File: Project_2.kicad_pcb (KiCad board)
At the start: 4 copper layers, 82 x 58.4 mm, 154 parts, among them CON3 BARREL_JACK, J1 USB, P1 CONN_01X10, P2 CONN_01X02, Q1 RTQ020N03, Q2 RTQ020N03, Q3 RTQ020N03, Q4 RTQ020N03, Q5 RTQ020N03, U1 LM2675_Adj, U2 LM2675_5V, U3 SM72442, U4 SM72295, U5 TLV2371_DBV

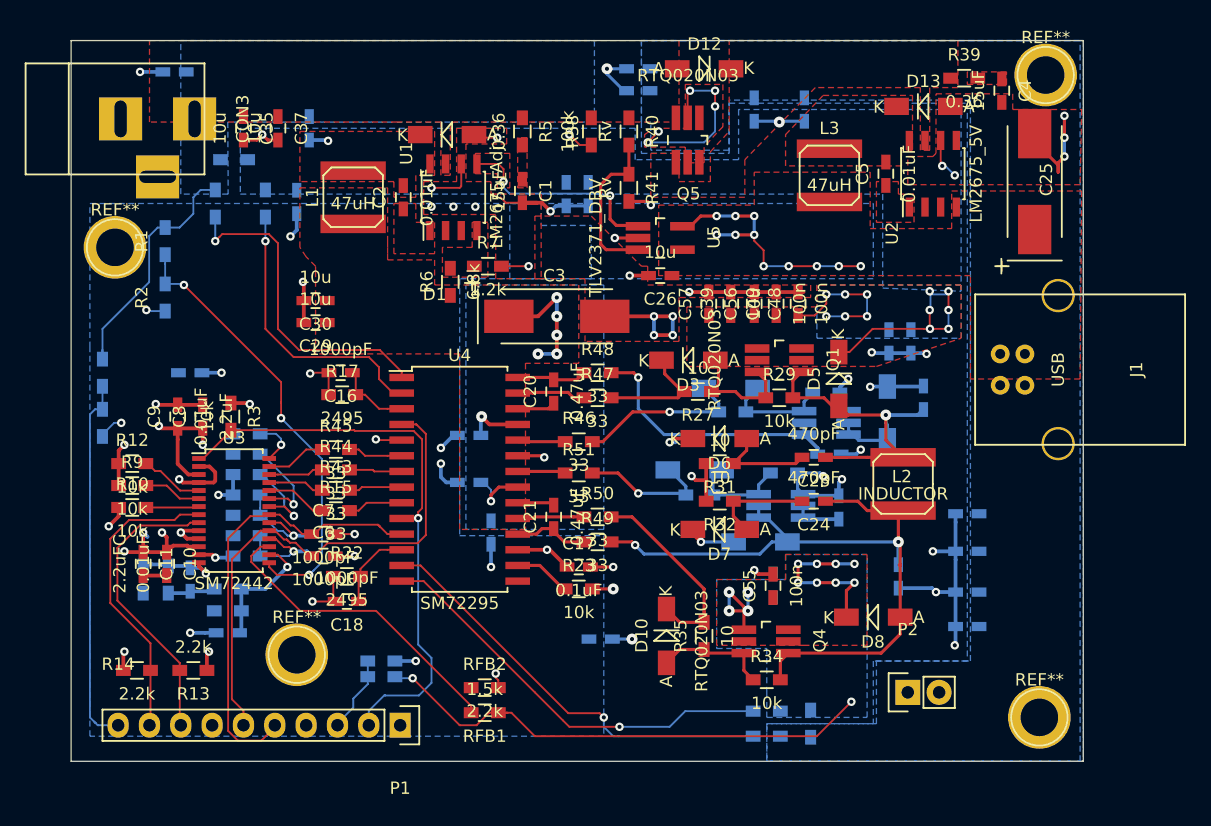
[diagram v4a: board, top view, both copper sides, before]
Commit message: Cleared all DRC errors.
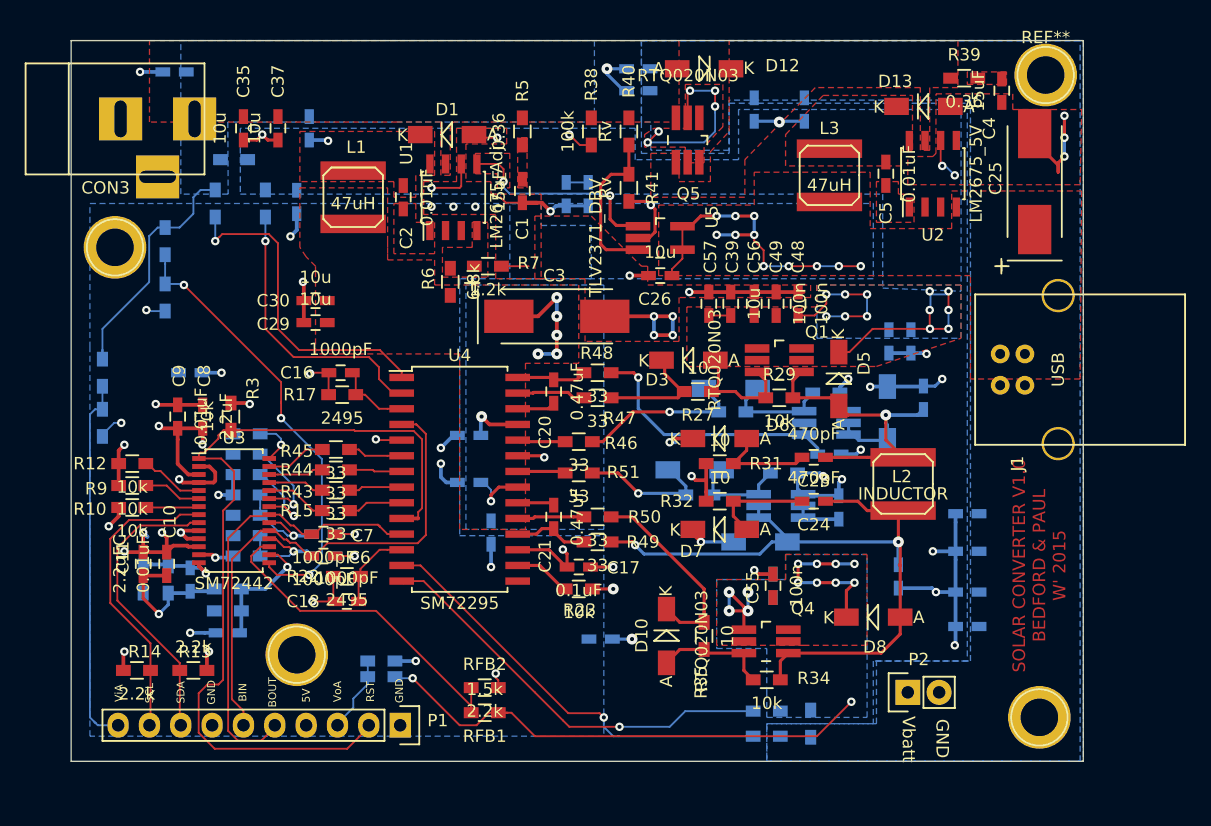
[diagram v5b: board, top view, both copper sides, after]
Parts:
- renumbered REF** to ?
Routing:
- net /Connectors/RST: track 48.4 -> 69.4 mm, vias 1 -> 0
- net GNDD: track 193.8 -> 201.8 mm, vias 63 -> 62
- net 5VDC: track 54.7 -> 60.3 mm
- net Vin: track 28.6 -> 32.2 mm
- net Net-(RFB1-Pad2): track 25.4 -> 27.4 mm
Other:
- board text added: "5V"
- board text added: "BIN"
- board text added: "BOUT"
- board text added: "GND"
- board text added: "RST"
- board text added: "SCL"
- board text added: "SDA"
- board text added: "SOLAR CONVERTER V1.0 BEDFORD & PAUL W' 2015"
- board text added: "Vbatt"
- board text added: "ViA"
- board text added: "VoA"

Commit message: updated via placement for better ground plane continuity
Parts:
- moved ? 1.09 mm to (135.4, 137.8)
- moved REF** 0.77 mm to (135.6, 85.5)
- moved C25 0.40 mm to (133.9, 94.4)
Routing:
- net 8VDC: track 20.5 -> 30.2 mm, vias 7 -> 8
- net GNDD: track 201.8 -> 206.9 mm
- net /HBridge/HSA: track 52.5 -> 56.1 mm
- net /HBridge/HSB: track 63.5 -> 67.1 mm
- net 5VDC: track 60.3 -> 57.5 mm, vias 21 -> 18
- net Vin: track 32.2 -> 29.4 mm, vias 12 -> 10
- net Vout: track 63.0 -> 65.2 mm
- net (no net): track 0.72 -> 0.00 mm
- net Vbatt: track 14.7 -> 14.2 mm
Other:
- board size 82 x 58.4 mm -> 82.7 x 58.4 mm
